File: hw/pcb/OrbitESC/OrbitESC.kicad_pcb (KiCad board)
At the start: 4 copper layers, 75 x 30 mm, 225 parts, among them J1 USB_C_Receptacle_USB2.0, J11 VDC, J12 GND, J2 Micro_SD_Card_Det, J3 TermA, J4 TermB, J5 TermC, J6 CAN1, J7 Serial1, J8 Serial2, J9 CAN2, Q1 MCAC80N10Y, Q2 MCAC80N10Y, Q3 MCAC80N10Y, Q4 MCAC80N10Y, Q5 MCAC80N10Y, Q6 MCAC80N10Y, Q7 2N7002, SW1 Reset, SW2 User, SW3 Boot, SW4 Break, U1 TLE9250X, U10 TLE9250X, U2 AT25SF081-SSHD-X, U3 24LC128, U4 STM32F446ZCHx, U5 DRV8300DRGER, U6 TSV994, U7 AP62200Z6-7, U8 AP2171W, U9 AP2120, X1 ECS-2520MV-240-BN

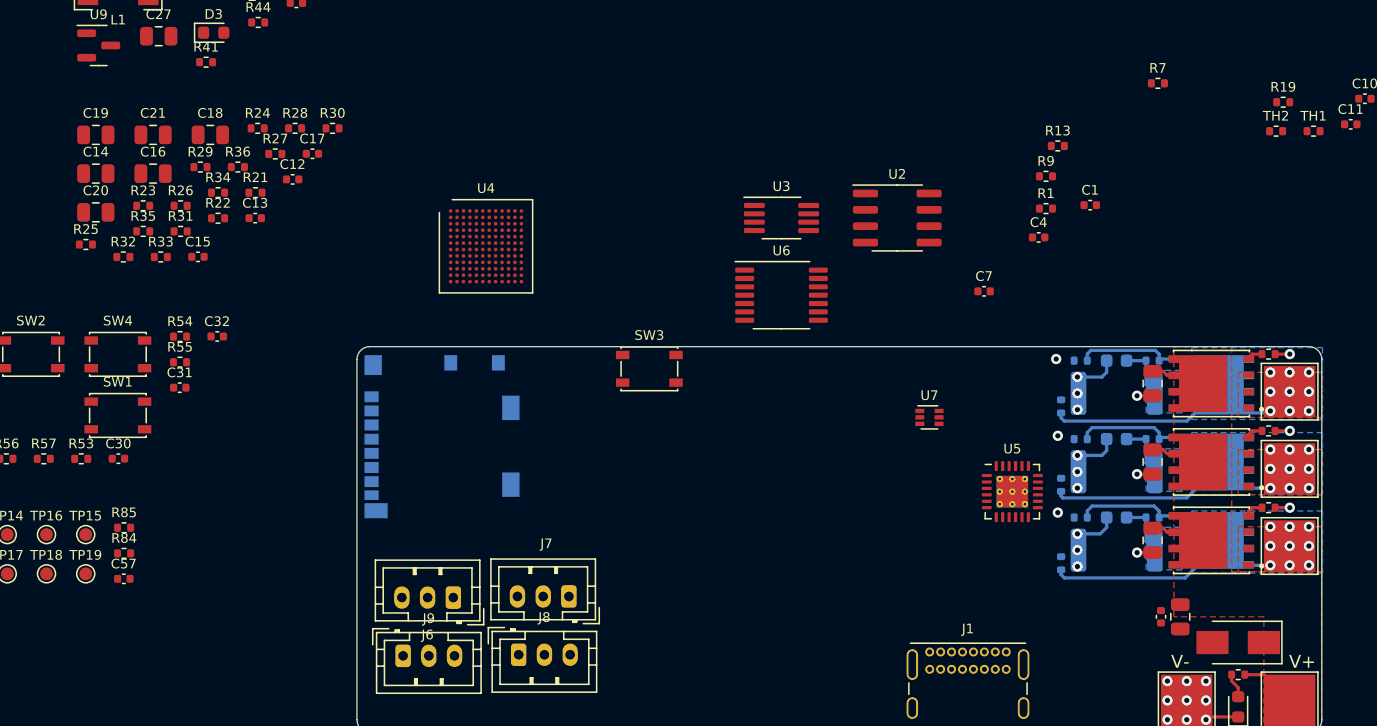
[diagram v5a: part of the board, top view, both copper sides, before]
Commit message: rework power stage
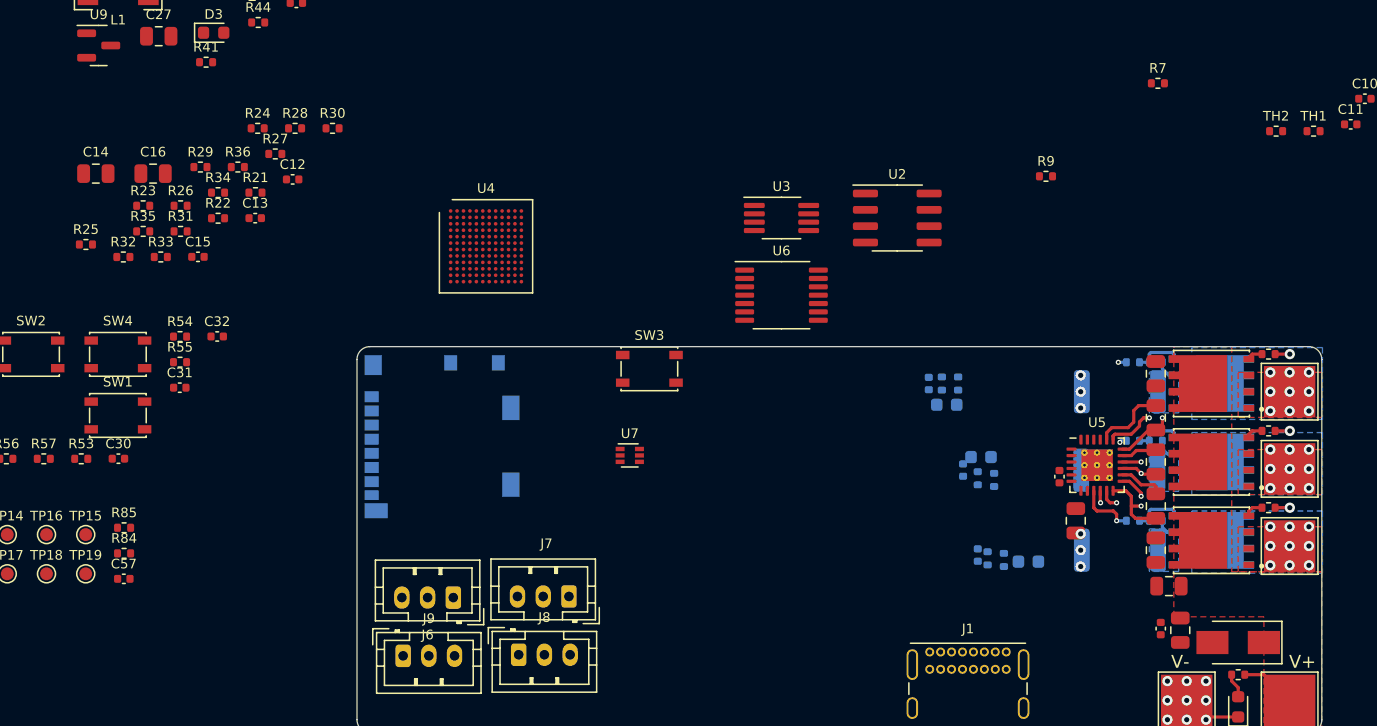
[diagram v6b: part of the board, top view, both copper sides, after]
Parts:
- C1, C4, C7, R1, R13, R19: moved to B.Cu
- moved C19 85.3 mm to (165.1, 89.5), turned to -90 degrees
- moved C20 84.7 mm to (165.1, 93.0), turned to -90 degrees
- moved C21 83.1 mm to (165.1, 96.4), turned to -90 degrees
- moved C18 73.7 mm to (158.9, 97.5), turned to -90 degrees
- moved C17 63.3 mm to (157.6, 94.1), turned to 90 degrees
- moved R19 42.3 mm to (152.0, 100.5), turned to -90 degrees
- moved R13 26.6 mm to (151.3, 94.2), turned to -90 degrees
- moved U7 23.5 mm to (124.2, 92.5)
- moved C7 20.5 mm to (151.3, 100.2), turned to 90 degrees
- moved C4 19.0 mm to (150.1, 93.6), turned to 90 degrees
- moved C1 18.7 mm to (147.4, 86.9), turned to 90 degrees
- moved R1 15.8 mm to (148.5, 86.9), turned to -90 degrees
- moved C2 13.6 mm to (148.8, 88.5)
- moved C5 10.6 mm to (151.5, 92.6)
- moved C6 9.74 mm to (166.1, 102.6), turned to 180 degrees
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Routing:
- net /Outputs and Shunts/GDL_A: track 0.00 -> 14.9 mm, vias 0 -> 2
- net GND: track 16.4 -> 4.59 mm, vias 21 -> 15
- net /Outputs and Shunts/GDL_B: track 0.00 -> 7.42 mm, vias 0 -> 2
- net Net-(C19-Pad1): track 0.00 -> 5.76 mm
- net VDC: track 9.67 -> 4.32 mm
- net /Outputs and Shunts/GDL_C: track 0.00 -> 4.57 mm, vias 0 -> 1
- net Net-(Q4-Pad2): track 8.13 -> 3.79 mm
- net Net-(Q2-Pad2): track 8.05 -> 3.79 mm
- net Net-(Q6-Pad2): track 8.13 -> 3.92 mm
- net /Outputs and Shunts/GDH_C: track 19.3 -> 15.1 mm
- net /Outputs and Shunts/SH_B: track 17.0 -> 13.0 mm, vias 9 -> 10
- net /Outputs and Shunts/SH_A: track 17.1 -> 13.3 mm, vias 9 -> 10
- net Net-(C21-Pad1): track 0.00 -> 3.53 mm
- net /Outputs and Shunts/GDH_B: track 19.3 -> 16.0 mm
- net Net-(C20-Pad1): track 0.00 -> 2.77 mm
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
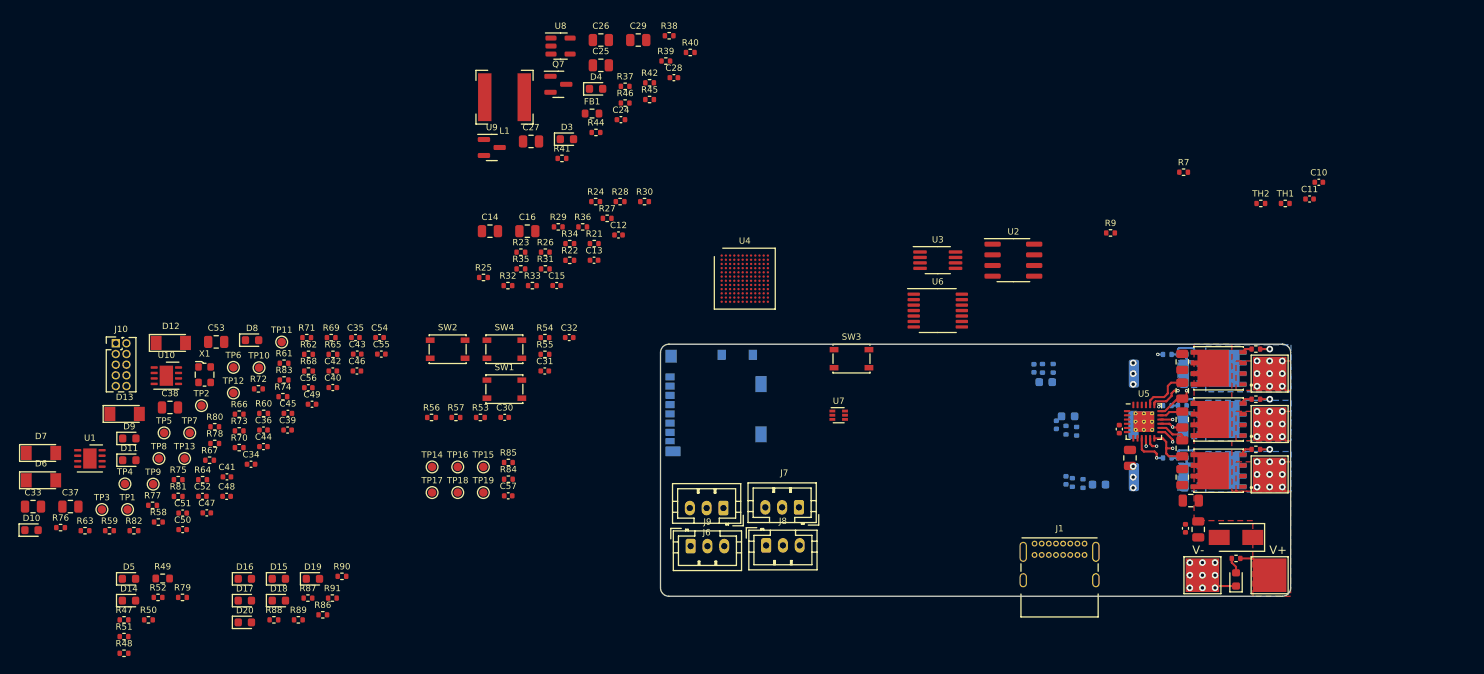
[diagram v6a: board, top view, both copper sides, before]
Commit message: Redo power stage layout. Start on power supplies
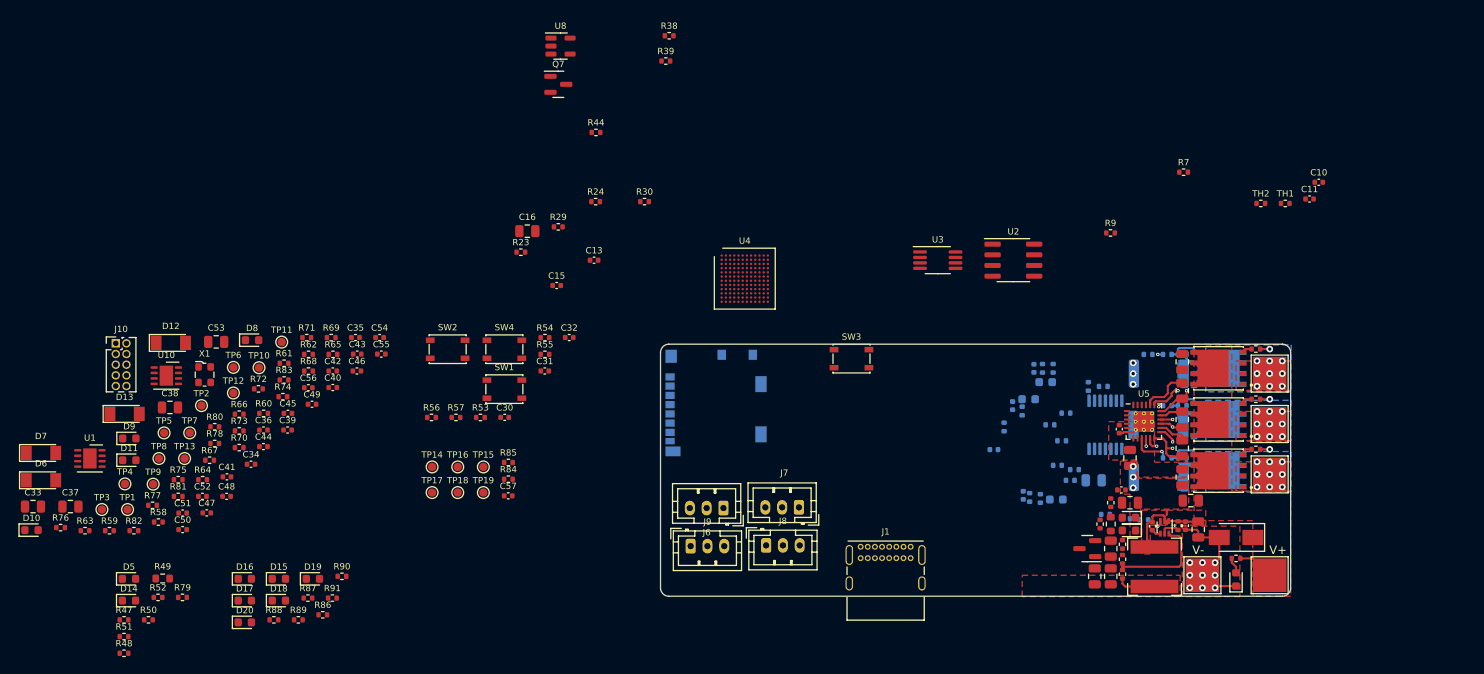
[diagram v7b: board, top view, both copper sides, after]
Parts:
- C12, C14, R21, R22, R25, R26, R27, R28, R31, R32, R33, R34, R35, R36, U6: moved to B.Cu
- moved L1 95.4 mm to (161.8, 110.5), turned to -90 degrees
- moved C26 86.8 mm to (154.7, 111.6), turned to 90 degrees
- moved C25 85.9 mm to (156.6, 111.6), turned to 90 degrees
- moved U9 85.5 mm to (153.8, 108.3), turned to 180 degrees
- moved R37 84.0 mm to (164.6, 105.6), turned to -90 degrees
- moved C27 83.3 mm to (158.9, 102.9), turned to 180 degrees
- moved C29 82.6 mm to (156.6, 108.3), turned to 90 degrees
- moved R41 82.0 mm to (158.0, 109.6), turned to -90 degrees
- moved D3 81.5 mm to (158.8, 106.2), turned to 180 degrees
- moved D4 81.4 mm to (158.8, 104.6), turned to 180 degrees
- moved R40 80.6 mm to (158.0, 111.4), turned to 90 degrees
- moved C24 79.6 mm to (161.5, 105.7), turned to -90 degrees
- moved R25 79.2 mm to (156.0, 104.3), turned to 180 degrees
- moved FB1 78.7 mm to (156.6, 105.4), turned to 90 degrees
- moved R26 78.0 mm to (160.5, 104.9), turned to 180 degrees
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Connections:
- U6 pad 1: /MCU/MOTOR_IC -> /MCU/MOTOR_IA
- U6 pad 2: Net-(R25-Pad2) -> Net-(R34-Pad2)
- U6 pad 6: Net-(R34-Pad2) -> Net-(R31-Pad2)
- U6 pad 7: /MCU/MOTOR_IA -> /MCU/MOTOR_IB
- U6 pad 8: /MCU/MOTOR_IB -> /MCU/MOTOR_IC
- U6 pad 9: Net-(R31-Pad2) -> Net-(R25-Pad2)
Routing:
- net Net-(R40-Pad2): track 0.00 -> 12.7 mm
- net GND: track 4.59 -> 15.5 mm, vias 15 -> 16
- net Net-(C24-Pad1): track 0.00 -> 6.60 mm
- net +5V: track 0.00 -> 4.57 mm
- net VDC: track 4.32 -> 7.86 mm
- net Net-(R37-Pad2): track 0.00 -> 2.29 mm
- net Net-(C24-Pad2): track 0.00 -> 1.14 mm
- added copper zone on F.Cu, net +5V
- added copper zone on F.Cu, net GND
- added copper zone on F.Cu, net Net-(C24-Pad1)

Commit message: Sync
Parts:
- moved R33 9.37 mm to (157.5, 89.0)
- moved R26 7.92 mm to (160.0, 97.0), turned to 90 degrees
- moved R27 6.79 mm to (156.5, 98.2), turned to 90 degrees
- moved R25 6.21 mm to (157.5, 98.2), turned to 90 degrees
- moved R21 4.51 mm to (154.8, 98.2), turned to -90 degrees
- moved C14 3.02 mm to (152.5, 98.0), turned to -90 degrees
- moved R28 2.94 mm to (152.5, 96.0), turned to 0 degrees
- moved R22 2.78 mm to (153.8, 98.2), turned to 90 degrees
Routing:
- net ISenseVRef: track 0.00 -> 14.6 mm
- net GND: track 15.5 -> 23.0 mm, vias 16 -> 22
- net /Outputs and Shunts/C_ISENSE_P: track 1.57 -> 8.82 mm
- net Net-(R25-Pad2): track 0.00 -> 5.58 mm
- net +5V: track 4.57 -> 9.70 mm
- net Net-(C14-Pad1): track 0.00 -> 3.80 mm
- net Net-(D4-Pad2): track 0.00 -> 3.17 mm
- net /MCU/MOTOR_IC: track 0.00 -> 3.04 mm
- net Net-(R21-Pad1): track 0.00 -> 2.51 mm
- net Net-(FB1-Pad2): track 0.00 -> 1.20 mm
- net Net-(D3-Pad2): track 0.00 -> 1.15 mm
- net +3.3VADC: track 0.00 -> 0.49 mm, vias 0 -> 5
- added copper zone on F.Cu, net +3.3VADC
- added copper zone on In2.Cu, net +3.3VADC
